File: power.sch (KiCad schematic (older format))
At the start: 75 parts, among them J5 VJ1, Q1 BC857, Q2 2N7002, U1 LFE5U-45F-6BG381C, U3 TLV62569DBV, U4 TLV62569DBV, U5 TLV62569DBV, U7 PCF8523, Y2 32768Hz

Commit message: schematics: diodes new footprints
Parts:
- D11: footprint LEDs:LED_0805 -> LED_SMD:LED_0805_2012Metric
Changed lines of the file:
@@
 F 0 "D11" H 4850 4300 50  0000 C CNN
 F 1 "RED" H 4850 4100 50  0000 C CNN
-F 2 "LEDs:LED_0805" H 4850 4200 50  0001 C CNN
+F 2 "LED_SMD:LED_0805_2012Metric" H 4850 4200 50  0001 C CNN
 F 3 "" H 4850 4200 50  0000 C CNN
 	1    4850 4200

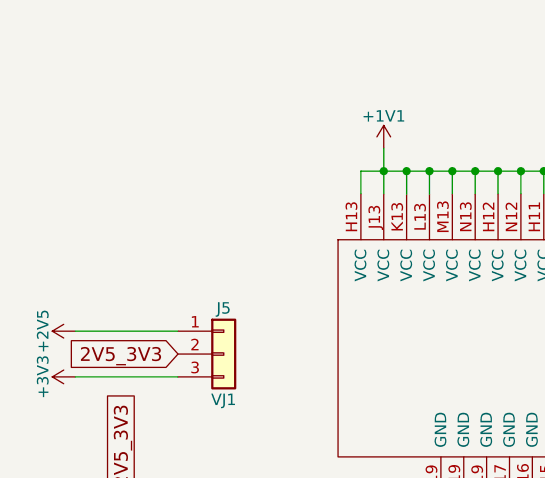
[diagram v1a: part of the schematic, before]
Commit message: schematics: RP4,5 0R jumpers for factory default 2.5/3.3V voltage setting
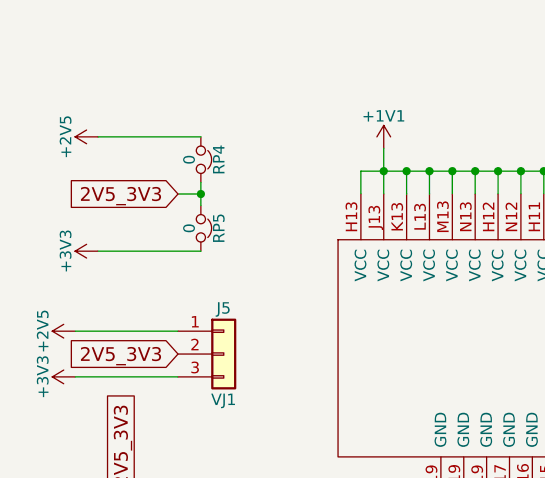
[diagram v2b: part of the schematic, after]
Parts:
- added RP4, RP5: 0, Resistor_SMD:R_0603_1608Metric_Pad0.84x1.00mm_HandSolder, symbol ulx3s-rescue:Jumper_NC_Small
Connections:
- net +2V5: now also RP4.1
- net +3V3: now also RP5.2
- net 2V5_3V3: now also RP4.2, RP5.1
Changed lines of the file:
@@
 Wire Wire Line
 	2400 4200 2400 4250
+$Comp
+L ulx3s-rescue:Jumper_NC_Small RP4
+U 1 1 5AF31FAC
+P 1300 1000
+F 0 "RP4" H 1300 1080 50  0000 C CNN
+F 1 "0" H 1300 950 50  0000 C CNN
+F 2 "Resistor_SMD:R_0603_1608Metric_Pad0.84x1.00mm_HandSolder" H 1300 1000 50  0001 C CNN
+F 3 "" H 1300 1000 50  0001 C CNN
+F 4 "www.mouser.com" H 1300 1000 60  0001 C CNN "Distributor1_URL"
+F 5 "Do not install" H 1300 1000 50  0001 C CNN "Note"
+	1    1300 1000
+	0    1    1    0
+$EndComp
+$Comp
+L ulx3s-rescue:Jumper_NC_Small RP5
+U 1 1 5AF3694A
+P 1300 1300
+F 0 "RP5" H 1300 1380 50  0000 C CNN
+F 1 "0" H 1300 1250 50  0000 C CNN
+F 2 "Resistor_SMD:R_0603_1608Metric_Pad0.84x1.00mm_HandSolder" H 1300 1300 50  0001 C CNN
+F 3 "" H 1300 1300 50  0001 C CNN
+F 4 "www.mouser.com" H 1300 1300 60  0001 C CNN "Distributor1_URL"
+F 5 "Do not install" H 1300 1300 50  0001 C CNN "Note"
+	1    1300 1300
+	0    1    1    0
+$EndComp
+Text GLabel 1200 1150 0    60   Input ~ 0
+2V5_3V3
+$Comp
+L power:+2V5 #PWR0169
+U 1 1 5AF3DD8E
+P 850 900
+F 0 "#PWR0169" H 850 750 50  0001 C CNN
+F 1 "+2V5" H 850 1040 50  0000 C CNN
+F 2 "" H 850 900 50  0001 C CNN
+F 3 "" H 850 900 50  0001 C CNN
+	1    850  900
+	0    -1   -1   0
+$EndComp
+$Comp
+L power:+3V3 #PWR0170
+U 1 1 5AF3DD94
+P 850 1400
+F 0 "#PWR0170" H 850 1250 50  0001 C CNN
+F 1 "+3V3" H 850 1540 50  0000 C CNN
+F 2 "" H 850 1400 50  0001 C CNN
+F 3 "" H 850 1400 50  0001 C CNN
+	1    850  1400
+	0    -1   -1   0
+$EndComp
+Wire Wire Line
+	850  900  1300 900
+Wire Wire Line
+	850  1400 1300 1400
+Wire Wire Line
+	1200 1150 1300 1150
+Wire Wire Line
+	1300 1150 1300 1100
+Wire Wire Line
+	1300 1150 1300 1200
+Connection ~ 1300 1150
 $EndSCHEMATC

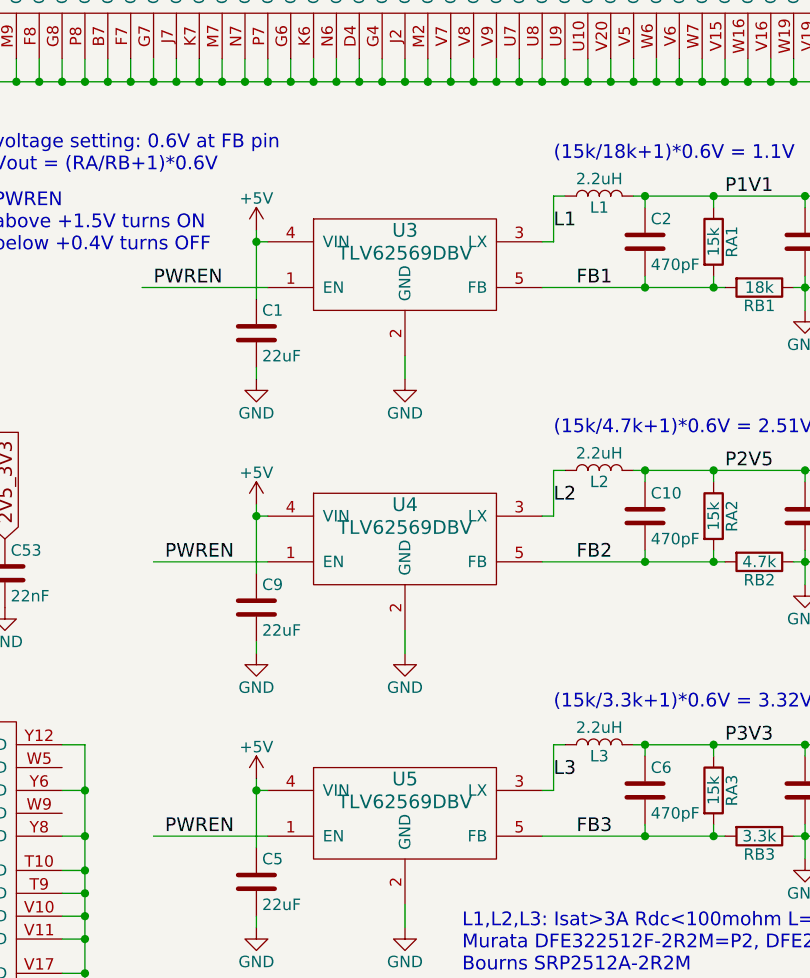
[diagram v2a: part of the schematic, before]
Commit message: schematics: using generic DCDC converter symbol
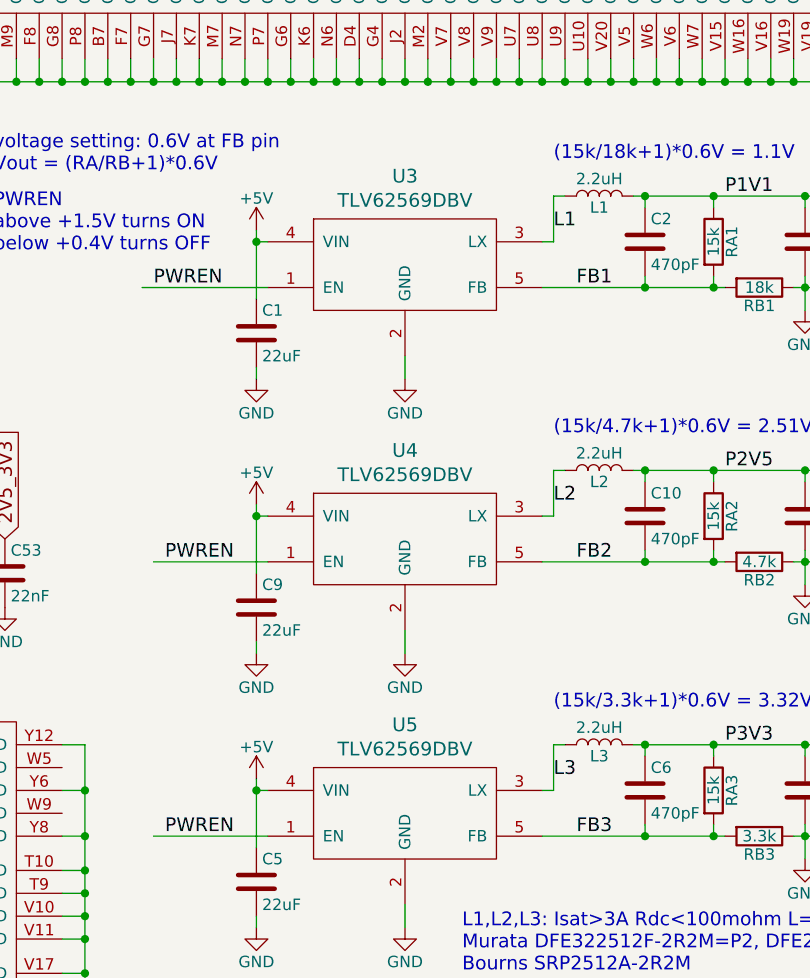
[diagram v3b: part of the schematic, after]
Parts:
- removed U3, U4, U5: TLV62569DBV, TSOT-25:TSOT-25, symbol ap3429a:AP3429A
- added U3, U4, U5: TLV62569DBV, TSOT-25:TSOT-25, symbol dcdc:DCDC
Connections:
- net +5V: now also U3.4 (VIN), U4.4 (VIN), U5.4 (VIN)
- net FB1: now also U3.5 (FB)
- net FB2: now also U4.5 (FB)
- net FB3: now also U5.5 (FB)
- net GND: now also U3.2 (GND), U4.2 (GND), U5.2 (GND)
- net L1: now also U3.3 (LX)
- net L2: now also U4.3 (LX)
- net L3: now also U5.3 (LX)
- net PWREN: now also U3.1 (EN), U4.1 (EN), U5.1 (EN)
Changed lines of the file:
@@
 voltage setting: 0.6V at FB pin\nVout = (RA/RB+1)*0.6V\n
-$Comp
-L ap3429a:AP3429A U5
-U 1 1 58D67BBA
-P 8050 5800
-F 0 "U5" H 8050 5950 60  0000 C CNN
-F 1 "TLV62569DBV" H 8050 5850 60  0000 C CNN
-F 2 "TSOT-25:TSOT-25" H 8050 5800 60  0001 C CNN
-F 3 "http://www.ti.com/lit/ds/symlink/tlv62569.pdf" H 8050 5800 60  0001 C CNN
-F 4 "www.ti.com" H 8050 5800 60  0001 C CNN "MFG_URL"
-F 5 "TLV62569DBV" H 8050 5800 60  0001 C CNN "MFG_PN"
-F 6 "www.mouser.com" H 8050 5800 60  0001 C CNN "Distributor1_URL"
-F 7 "595-TLV62569DBVR" H 8050 5800 60  0001 C CNN "Distributor1_PN"
-	1    8050 5800
-	1    0    0    -1
-$EndComp
 $Comp
 L power:GND #PWR073
@@
 	1    0    0    -1
 $EndComp
-$Comp
-L ap3429a:AP3429A U4
-U 1 1 5A57BC36
-P 8050 4600
-F 0 "U4" H 8050 4750 60  0000 C CNN
-F 1 "TLV62569DBV" H 8050 4650 60  0000 C CNN
-F 2 "TSOT-25:TSOT-25" H 8050 4600 60  0001 C CNN
-F 3 "http://www.ti.com/lit/ds/symlink/tlv62569.pdf" H 8050 4600 60  0001 C CNN
-F 4 "www.ti.com" H 8050 4600 60  0001 C CNN "MFG_URL"
-F 5 "TLV62569DBV" H 8050 4600 60  0001 C CNN "MFG_PN"
-F 6 "www.mouser.com" H 8050 4600 60  0001 C CNN "Distributor1_URL"
-F 7 "595-TLV62569DBVR" H 8050 4600 60  0001 C CNN "Distributor1_PN"
-	1    8050 4600
-	1    0    0    -1
-$EndComp
-$Comp
-L ap3429a:AP3429A U3
-U 1 1 5A57BFD7
-P 8050 3400
-F 0 "U3" H 8050 3550 60  0000 C CNN
-F 1 "TLV62569DBV" H 8050 3450 60  0000 C CNN
-F 2 "TSOT-25:TSOT-25" H 8050 3400 60  0001 C CNN
-F 3 "http://www.ti.com/lit/ds/symlink/tlv62569.pdf" H 8050 3400 60  0001 C CNN
-F 4 "www.ti.com" H 8050 3400 60  0001 C CNN "MFG_URL"
-F 5 "TLV62569DBV" H 8050 3400 60  0001 C CNN "MFG_PN"
-F 6 "www.mouser.com" H 8050 3400 60  0001 C CNN "Distributor1_URL"
-F 7 "595-TLV62569DBVR" H 8050 3400 60  0001 C CNN "Distributor1_PN"
-	1    8050 3400
-	1    0    0    -1
-$EndComp
 Text Notes 7900 1200 0    60   ~ 0
 Decoupling capacitors: see Lattice\nPower Decoupling and Bypass Filtering for Programmable Devices
@@
 	1300 1150 1300 1200
 Connection ~ 1300 1150
+$Comp
+L dcdc:DCDC U3
+U 1 1 5AF563F3
+P 8050 3400
+F 0 "U3" H 8050 3787 60  0000 C CNN
+F 1 "TLV62569DBV" H 8050 3681 60  0000 C CNN
+F 2 "TSOT-25:TSOT-25" H 8050 3400 60  0001 C CNN
+F 3 "http://www.ti.com/lit/ds/symlink/tlv62569.pdf" H 8050 3400 60  0001 C CNN
+F 4 "www.ti.com" H 8050 3400 50  0001 C CNN "MFG_URL"
+F 5 "TLV62569DBVR" H 8050 3400 50  0001 C CNN "MFG_PN"
+F 6 "www.mouser.com" H 8050 3400 50  0001 C CNN "Distributor1_URL"
+F 7 "595-TLV62569DBVR" H 8050 3400 50  0001 C CNN "Distributor1_PN"
+	1    8050 3400
+	1    0    0    -1
+$EndComp
+$Comp
+L dcdc:DCDC U4
+U 1 1 5AFCB5C1
+P 8050 4600
+F 0 "U4" H 8050 4987 60  0000 C CNN
+F 1 "TLV62569DBV" H 8050 4881 60  0000 C CNN
+F 2 "TSOT-25:TSOT-25" H 8050 4600 60  0001 C CNN
+F 3 "http://www.ti.com/lit/ds/symlink/tlv62569.pdf" H 8050 4600 60  0001 C CNN
+F 4 "www.ti.com" H 8050 4600 50  0001 C CNN "MFG_URL"
+F 5 "TLV62569DBVR" H 8050 4600 50  0001 C CNN "MFG_PN"
+F 6 "www.mouser.com" H 8050 4600 50  0001 C CNN "Distributor1_URL"
+F 7 "595-TLV62569DBVR" H 8050 4600 50  0001 C CNN "Distributor1_PN"
+	1    8050 4600
+	1    0    0    -1
+$EndComp
+$Comp
+L dcdc:DCDC U5
+U 1 1 5AFCC283
+P 8050 5800
+F 0 "U5" H 8050 6187 60  0000 C CNN
+F 1 "TLV62569DBV" H 8050 6081 60  0000 C CNN
+F 2 "TSOT-25:TSOT-25" H 8050 5800 60  0001 C CNN
+F 3 "http://www.ti.com/lit/ds/symlink/tlv62569.pdf" H 8050 5800 60  0001 C CNN
+F 4 "www.ti.com" H 8050 5800 50  0001 C CNN "MFG_URL"
+F 5 "TLV62569DBVR" H 8050 5800 50  0001 C CNN "MFG_PN"
+F 6 "www.mouser.com" H 8050 5800 50  0001 C CNN "Distributor1_URL"
+F 7 "595-TLV62569DBVR" H 8050 5800 50  0001 C CNN "Distributor1_PN"
+	1    8050 5800
+	1    0    0    -1
+$EndComp
 $EndSCHEMATC

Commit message: schematics: replace 45F chip with 85F
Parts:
- U1: value LFE5U-45F-6BG381C -> LFE5U-85F-6BG381C; symbol lfe5bg381:LFE5U-45F-6BG381C -> lfe5bg381:LFE5U-85F-6BG381C; Distributor1_PN 842-LFE5U45F6BG381C -> 842-LFE5U85F6BG381C; MFG_PN LFE5U-45F-6BG381C -> LFE5U-85F-6BG381C
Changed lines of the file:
@@
 WARNING\nECP5 family datasheet\np.48: Power Supply Ramp rates\nfor all supplies 0.01-10V/ms\n
 $Comp
-L lfe5bg381:LFE5U-45F-6BG381C U1
+L lfe5bg381:LFE5U-85F-6BG381C U1
 U 8 1 5A076CD7
 P 5700 6400
@@
 AR Path="/58D51CAD/5A076CD7" Ref="U1"  Part="8"
 F 0 "U1" H 5700 7350 60  0000 C CNN
-F 1 "LFE5U-45F-6BG381C" H 5700 7250 60  0000 C CNN
+F 1 "LFE5U-85F-6BG381C" H 5700 7250 60  0000 C CNN
 F 2 "lfe5bg381:BGA-381_pitch0.8mm_dia0.4mm" H 4650 7350 60  0001 C CNN
 F 3 "http://www.latticesemi.com/~/media/LatticeSemi/Documents/ApplicationNotes/EH/TN1261.pdf?document_id=50463" H 4650 7350 60  0001 C CNN
-F 4 "LFE5U-45F-6BG381C" H 5700 6400 60  0001 C CNN "MFG_PN"
+F 4 "LFE5U-85F-6BG381C" H 5700 6400 60  0001 C CNN "MFG_PN"
 F 5 "www.mouser.com" H 5700 6400 60  0001 C CNN "Distributor1_URL"
-F 6 "842-LFE5U45F6BG381C" H 5700 6400 60  0001 C CNN "Distributor1_PN"
+F 6 "842-LFE5U85F6BG381C" H 5700 6400 60  0001 C CNN "Distributor1_PN"
 	8    5700 6400
 	1    0    0    -1
 $EndComp
 $Comp
-L lfe5bg381:LFE5U-45F-6BG381C U1
+L lfe5bg381:LFE5U-85F-6BG381C U1
 U 9 1 5A077765
 P 6200 1800
@@
 AR Path="/58D51CAD/5A077765" Ref="U1"  Part="9"
 F 0 "U1" H 6200 2750 60  0000 C CNN
-F 1 "LFE5U-45F-6BG381C" H 6200 2650 60  0000 C CNN
+F 1 "LFE5U-85F-6BG381C" H 6200 2650 60  0000 C CNN
 F 2 "lfe5bg381:BGA-381_pitch0.8mm_dia0.4mm" H 5150 2750 60  0001 C CNN
-F 3 "http://www.latticesemi.com/~/media/LatticeSemi/Documents/DataSheets/ECP5/FPGA-DS-02012.pdf" H 5150 2750 60  0001 C CNN
+F 3 "http://www.latticesemi.com/~/media/LatticeSemi/Documents/ApplicationNotes/EH/TN1261.pdf?document_id=50463" H 5150 2750 60  0001 C CNN
 F 4 "www.latticesemi.com" H 6200 1800 60  0001 C CNN "MFG_URL"
-F 5 "LFE5U-45F-6BG381C" H 6200 1800 60  0001 C CNN "MFG_PN"
+F 5 "LFE5U-85F-6BG381C" H 6200 1800 60  0001 C CNN "MFG_PN"
 F 6 "www.mouser.com" H 6200 1800 60  0001 C CNN "Distributor1_URL"
-F 7 "842-LFE5U45F6BG381C" H 6200 1800 60  0001 C CNN "Distributor1_PN"
+F 7 "842-LFE5U85F6BG381C" H 6200 1800 60  0001 C CNN "Distributor1_PN"
 	9    6200 1800
 	1    0    0    -1

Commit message: schematics: BAT54 specified PN
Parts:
- D12, D15: Distributor1_PN (none) -> 621-BAT54WSQ-7-F; Distributor1_URL (none) -> www.mouser.com; MFG_PN (none) -> BAT54WSQ-7-F; MFG_URL (none) -> www.diodes.com
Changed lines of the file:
@@
-$EndComp
-$Comp
-L ulx3s-rescue:D_Schottky D15
-U 1 1 58D84D8A
-P 3100 5600
-F 0 "D15" H 3100 5700 50  0000 C CNN
-F 1 "BAT54W" H 3100 5500 50  0000 C CNN
-F 2 "Diodes_SMD:D_SOD-323_HandSoldering" H 3100 5600 50  0001 C CNN
-F 3 "" H 3100 5600 50  0000 C CNN
-	1    3100 5600
-	-1   0    0    1
 $EndComp
 $Comp
@@
 F 1 "BAT54W" H 3800 4850 50  0000 C CNN
 F 2 "Diodes_SMD:D_SOD-323_HandSoldering" H 3800 4950 50  0001 C CNN
-F 3 "" H 3800 4950 50  0000 C CNN
+F 3 "https://www.diodes.com/assets/Datasheets/ds30065.pdf" H 3800 4950 50  0001 C CNN
+F 4 "www.diodes.com" H 3800 4950 50  0001 C CNN "MFG_URL"
+F 5 "BAT54WSQ-7-F " H 3800 4950 50  0001 C CNN "MFG_PN"
+F 6 "www.mouser.com" H 3800 4950 50  0001 C CNN "Distributor1_URL"
+F 7 "621-BAT54WSQ-7-F " H 3800 4950 50  0001 C CNN "Distributor1_PN"
 	1    3800 4950
 	-1   0    0    1
@@
 	1    0    0    -1
 $EndComp
+$Comp
+L ulx3s-rescue:D_Schottky D15
+U 1 1 5AF673FF
+P 3100 5600
+F 0 "D15" H 3100 5700 50  0000 C CNN
+F 1 "BAT54W" H 3100 5500 50  0000 C CNN
+F 2 "Diodes_SMD:D_SOD-323_HandSoldering" H 3100 5600 50  0001 C CNN
+F 3 "https://www.diodes.com/assets/Datasheets/ds30065.pdf" H 3100 5600 50  0001 C CNN
+F 4 "www.diodes.com" H 3100 5600 50  0001 C CNN "MFG_URL"
+F 5 "BAT54WSQ-7-F " H 3100 5600 50  0001 C CNN "MFG_PN"
+F 6 "www.mouser.com" H 3100 5600 50  0001 C CNN "Distributor1_URL"
+F 7 "621-BAT54WSQ-7-F " H 3100 5600 50  0001 C CNN "Distributor1_PN"
+	1    3100 5600
+	-1   0    0    1
+$EndComp
 $EndSCHEMATC

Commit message: schematics: using battery footprint from project local library
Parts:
- BAT1: footprint Keystone_3000_2.5x12.5mm-CoinCell:Keystone_3000_1x12mm-CoinCell -> Keystone_3000_1x12mm-CoinCell:Keystone_3000_1x12mm-CoinCell
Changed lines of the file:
@@
 F 0 "BAT1" H 2450 4250 50  0000 L CNN
 F 1 "CR1225" V 2550 3850 50  0000 L CNN
-F 2 "Keystone_3000_2.5x12.5mm-CoinCell:Keystone_3000_1x12mm-CoinCell" V 2650 4160 50  0001 C CNN
+F 2 "Keystone_3000_1x12mm-CoinCell:Keystone_3000_1x12mm-CoinCell" V 2650 4160 50  0001 C CNN
 F 3 "http://www.keyelco.com/product-pdf.cfm?p=777" H 2650 4160 50  0001 C CNN
 F 4 "www.keyelco.com" H 2650 4100 60  0001 C CNN "MFG_URL"

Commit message: schematics: hopefully getting rid of all references to micro-gpdi-d
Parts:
- BTN0: symbol micro-hdmi-d:CONN_02X01 -> Switch:SW_Push
- J5: footprint Pin_Headers:Pin_Header_Angled_1x03_Pitch2.54mm -> Connector_PinHeader_2.54mm:PinHeader_1x03_P2.54mm_Horizontal; symbol ulx3s-rescue:Conn_01x03 -> Connector_Generic:Conn_01x03
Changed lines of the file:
@@
 L power:GND #PWR026
 U 1 1 58D72406
-P 1900 4600
-F 0 "#PWR026" H 1900 4350 50  0001 C CNN
-F 1 "GND" H 1900 4450 50  0000 C CNN
-F 2 "" H 1900 4600 50  0000 C CNN
-F 3 "" H 1900 4600 50  0000 C CNN
-	1    1900 4600
+P 2000 4600
+F 0 "#PWR026" H 2000 4350 50  0001 C CNN
+F 1 "GND" H 2000 4450 50  0000 C CNN
+F 2 "" H 2000 4600 50  0000 C CNN
+F 3 "" H 2000 4600 50  0000 C CNN
+	1    2000 4600
 	0    1    1    0
 $EndComp
@@
 BTN_PWRn
 $Comp
-L micro-hdmi-d:CONN_02X01 BTN0
+L Switch:SW_Push BTN0
 U 1 1 58E83FE0
-P 2150 4600
-F 0 "BTN0" H 2150 4700 50  0000 C CNN
-F 1 "PTS645" H 2150 4500 50  0000 C CNN
-F 2 "Buttons_Switches_SMD:SW_SPST_PTS645" H 2150 3400 50  0001 C CNN
-F 3 "http://www.ckswitches.com/media/1471/pts645.pdf" H 2150 3400 50  0001 C CNN
-F 4 "www.ckswitches.com" H 2150 4600 60  0001 C CNN "MFG_URL"
-F 5 "PTS645SL50SMTR92 LFS" H 2150 4600 60  0001 C CNN "MFG_PN"
-F 6 "www.mouser.com" H 2150 4600 60  0001 C CNN "Distributor1_URL"
-	1    2150 4600
-	-1   0    0    1
+P 2200 4600
+F 0 "BTN0" H 2200 4550 50  0000 C CNN
+F 1 "PTS645" H 2350 4700 50  0000 C CNN
+F 2 "Buttons_Switches_SMD:SW_SPST_PTS645" H 2200 3400 50  0001 C CNN
+F 3 "http://www.ckswitches.com/media/1471/pts645.pdf" H 2200 3400 50  0001 C CNN
+F 4 "www.ckswitches.com" H 2200 4600 60  0001 C CNN "MFG_URL"
+F 5 "PTS645SL50SMTR92 LFS" H 2200 4600 60  0001 C CNN "MFG_PN"
+F 6 "www.mouser.com" H 2200 4600 60  0001 C CNN "Distributor1_URL"
+	1    2200 4600
+	-1   0    0    -1
 $EndComp
 Wire Wire Line
@@
 2V5_3V3
 $Comp
-L ulx3s-rescue:Conn_01x03 J5
+L Connector_Generic:Conn_01x03 J5
 U 1 1 5AA2A24D
 P 1400 1850
@@
 F 0 "J5" H 1400 2050 50  0000 C CNN
 F 1 "VJ1" H 1400 1650 50  0000 C CNN
-F 2 "Pin_Headers:Pin_Header_Angled_1x03_Pitch2.54mm" H 1400 1850 50  0001 C CNN
+F 2 "Connector_PinHeader_2.54mm:PinHeader_1x03_P2.54mm_Horizontal" H 1400 1850 50  0001 C CNN
 F 3 "" H 1400 1850 50  0001 C CNN
 F 4 "www.mouser.com" H 1400 1850 60  0001 C CNN "Distributor1_URL"

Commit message: schematics: L1,L2,L3 changed footprint to fit DFE252012P-2R2M=P2
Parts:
- L1, L2, L3: footprint Resistors_SMD:R_1210_HandSoldering -> Inductor_SMD:L_Taiyo-Yuden_NR-24xx_HandSoldering
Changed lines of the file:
@@
 F 0 "L2" V 8850 4300 50  0000 C CNN
 F 1 "2.2uH" V 8975 4300 50  0000 C CNN
-F 2 "Resistors_SMD:R_1210_HandSoldering" H 8900 4300 50  0001 C CNN
+F 2 "Inductor_SMD:L_Taiyo-Yuden_NR-24xx_HandSoldering" H 8900 4300 50  0001 C CNN
 F 3 "http://psearch.en.murata.com/inductor/product/DFE252012PD-2R2M%23.pdf" H 8900 4300 50  0001 C CNN
 F 4 "www.murata.com" H 8900 4300 60  0001 C CNN "MFG_URL"
@@
 F 0 "L1" V 8850 3100 50  0000 C CNN
 F 1 "2.2uH" V 8975 3100 50  0000 C CNN
-F 2 "Resistors_SMD:R_1210_HandSoldering" H 8900 3100 50  0001 C CNN
+F 2 "Inductor_SMD:L_Taiyo-Yuden_NR-24xx_HandSoldering" H 8900 3100 50  0001 C CNN
 F 3 "http://psearch.en.murata.com/inductor/product/DFE252012PD-2R2M%23.pdf" H 8900 3100 50  0001 C CNN
 F 4 "www.murata.com" H 8900 3100 60  0001 C CNN "MFG_URL"
@@
 F 0 "L3" V 8850 5500 50  0000 C CNN
 F 1 "2.2uH" V 8975 5500 50  0000 C CNN
-F 2 "Resistors_SMD:R_1210_HandSoldering" H 8900 5500 50  0001 C CNN
+F 2 "Inductor_SMD:L_Taiyo-Yuden_NR-24xx_HandSoldering" H 8900 5500 50  0001 C CNN
 F 3 "http://psearch.en.murata.com/inductor/product/DFE252012PD-2R2M%23.pdf" H 8900 5500 50  0001 C CNN
 F 4 "www.murata.com" H 8900 5500 60  0001 C CNN "MFG_URL"
